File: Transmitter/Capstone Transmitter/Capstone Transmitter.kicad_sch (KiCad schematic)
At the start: 0 parts

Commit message: Started work on new schematics in KiCad
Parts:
- added BT1: Battery, Battery:BatteryHolder_Keystone_2479_3xAAA, symbol Device:Battery
- added C1, C2: C_Small, symbol Device:C_Small
- added U1: ESP32-C3-DevKitM-1, RF_Module:ESP32-C3-DevKitM-1, symbol RF_Module:ESP32-C3-DevKitM-1
- added U2: TPS63020DSJR, DSJ14_2P85X1P58, symbol TPS63020:TPS63020DSJR
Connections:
- new net: C1.1, C2.1, U2.10 (VIN), U2.11 (VIN)
- new net: U1.1 (GND), U1.12 (GND), U1.15 (GND), U1.16 (GND), U1.19 (GND), U1.24 (GND), U1.27 (GND), U1.30 (GND), U1.6 (GND), U1.8 (GND)
- new net: U1.13 (5V), U1.14 (5V)
- new net: U1.2 (3V3), U1.3 (3V3)
- new net +4.5V: BT1.1 (+)
- new net GND: BT1.2 (-)

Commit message: WIP remote
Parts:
- removed U1: ESP32-C3-DevKitM-1, RF_Module:ESP32-C3-DevKitM-1, symbol RF_Module:ESP32-C3-DevKitM-1
- added C10, C5, C6, C7, C8: 22u, symbol Device:C_Small
- added C11: 1U, symbol Device:C_Small
- added C3: 100n, symbol Device:C_Small
- added C4: 4p7, symbol Device:C_Small
- added C9: 0u1, symbol Device:C_Small
- added JP1: BootSel, symbol Jumper:Jumper_2_Small_Open
- added L1: 1u, symbol Device:L_Small
- added R1, R2: 1M, symbol Device:R_Small_US
- added R3: 68K, symbol Device:R_Small_US
- added R4: 180K, symbol Device:R_Small_US
- added R5: 10K, symbol Device:R_Small_US
- added U3: ESP32-WROOM-32UE, RF_Module:ESP32-WROOM-32UE, symbol RF_Module:ESP32-WROOM-32UE
- C1, C2: value C_Small -> 10u
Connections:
- net +4.5V: now also C1.1, C2.1, U2.10 (VIN), U2.11 (VIN)
- net GND: now also C1.2, C2.2, U2.15 (EPAD), U2.2 (GND), C10.2, C11.2, C3.2, C5.2, C6.2, C7.2, C8.2, C9.2, JP1.2 (B), R4.2, U3.[1,15,38,39] (GND)
- net EN: now reaches U2.1 (VINA)
- net EN: now also U2.12 (EN), C3.1
- net PS/SYNC: now reaches U2.13 (PS/SYNC)
- net at U2.14 (PG): now also R1.1
- net FB: now reaches U2.3 (FB)
- net FB: now also C4.2, R2.2, R4.1
- net +3.3V: now reaches U2.4 (VOUT)
- net +3.3V: now also U2.5 (VOUT), C10.1, C5.1, C6.1, C7.1, C8.1, C9.1, R1.2, R2.1, R3.1, R5.1, U3.2 (VDD)
- net L2: now reaches U2.6 (L2)
- net L2: now also U2.7 (L2), L1.2
- net L1: now reaches U2.8 (L1)
- net L1: now also U2.9 (L1), L1.1
- new net: JP1.1 (A), U3.25 (IO0)
- new net: C4.1, R3.2
- new net EN2: C11.1, R5.2, U3.3 (EN)
- new net UART_RX: U3.34 (RXD0/IO3)
- new net UART_TX: U3.35 (TXD0/IO1)
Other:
- moved on the sheet: BT1, C1, C2, U2

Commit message: Finished remote schematic, getting some sleep now
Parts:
- added J1, J2: Conn_01x04, symbol Connector_Generic:Conn_01x04
- added J3, J4, J5: Conn_01x02_Socket, symbol Connector:Conn_01x02_Socket
- added J6: AnalogStick Pot1 +/-, symbol Connector:Conn_01x02_Socket
- added J7: AnalogStick Pot2 +/-, symbol Connector:Conn_01x02_Socket
- added JP2: Pull up Jumper 1, symbol Jumper:Jumper_2_Small_Open
- added JP3: Pull up Jumper 2, symbol Jumper:Jumper_2_Small_Open
- added Q1: RevPolProt, symbol Transistor_FET:Q_PMOS_DGS
- added R6: 100K, symbol Device:R_Small_US
- added R7, R8: 10K, symbol Device:R_Small_US
- C11: value 1U -> 1u
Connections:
- net +3.3V: now also J1.1 (Pin_1), J6.1 (Pin_1), J7.1 (Pin_1), JP2.2 (B), JP3.2 (B)
- net +4.5V: now also Q1.3 (S); no longer BT1.1 (+)
- net GND: now also J1.4 (Pin_4), J6.2 (Pin_2), J7.2 (Pin_2), R6.2
- net UART_RX: now also J1.3 (Pin_3)
- net UART_TX: now also J1.2 (Pin_2)
- net JOY_BTN2: now reaches U3.11 (IO26)
- net JOY_BTN2: now also J5.1 (Pin_1)
- net JOY_BTN1: now reaches U3.12 (IO27)
- net JOY_BTN1: now also J5.2 (Pin_2)
- net JTAG_TMS: now reaches U3.13 (IO14)
- net JTAG_TMS: now also J2.1 (Pin_1)
- net JTAG_TDI: now reaches U3.14 (IO12)
- net JTAG_TDI: now also J2.2 (Pin_2)
- net JTAG_TCK: now reaches U3.16 (IO13)
- net JTAG_TCK: now also J2.3 (Pin_3)
- net JTAG_TDO: now reaches U3.23 (IO15)
- net JTAG_TDO: now also J2.4 (Pin_4)
- net JOY_X/LEFT: now reaches U3.6 (IO34)
- net JOY_X/LEFT: now also J3.1 (Pin_1), R8.1
- net JOY_Y/RIGHT: now reaches U3.7 (IO35)
- net JOY_Y/RIGHT: now also J3.2 (Pin_2), R7.1
- net JOY_UP: now reaches U3.8 (IO32)
- net JOY_UP: now also J4.1 (Pin_1)
- net JOY_DOWN: now reaches U3.9 (IO33)
- net JOY_DOWN: now also J4.2 (Pin_2)
- new net: JP2.1 (A), R8.2
- new net: BT1.1 (+), Q1.1 (D)
- new net: Q1.2 (G), R6.1
- new net: JP3.1 (A), R7.2
- no-connect marks 0 -> 13
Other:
- moved on the sheet: BT1, C10, C11, C9, JP1, R5, U3

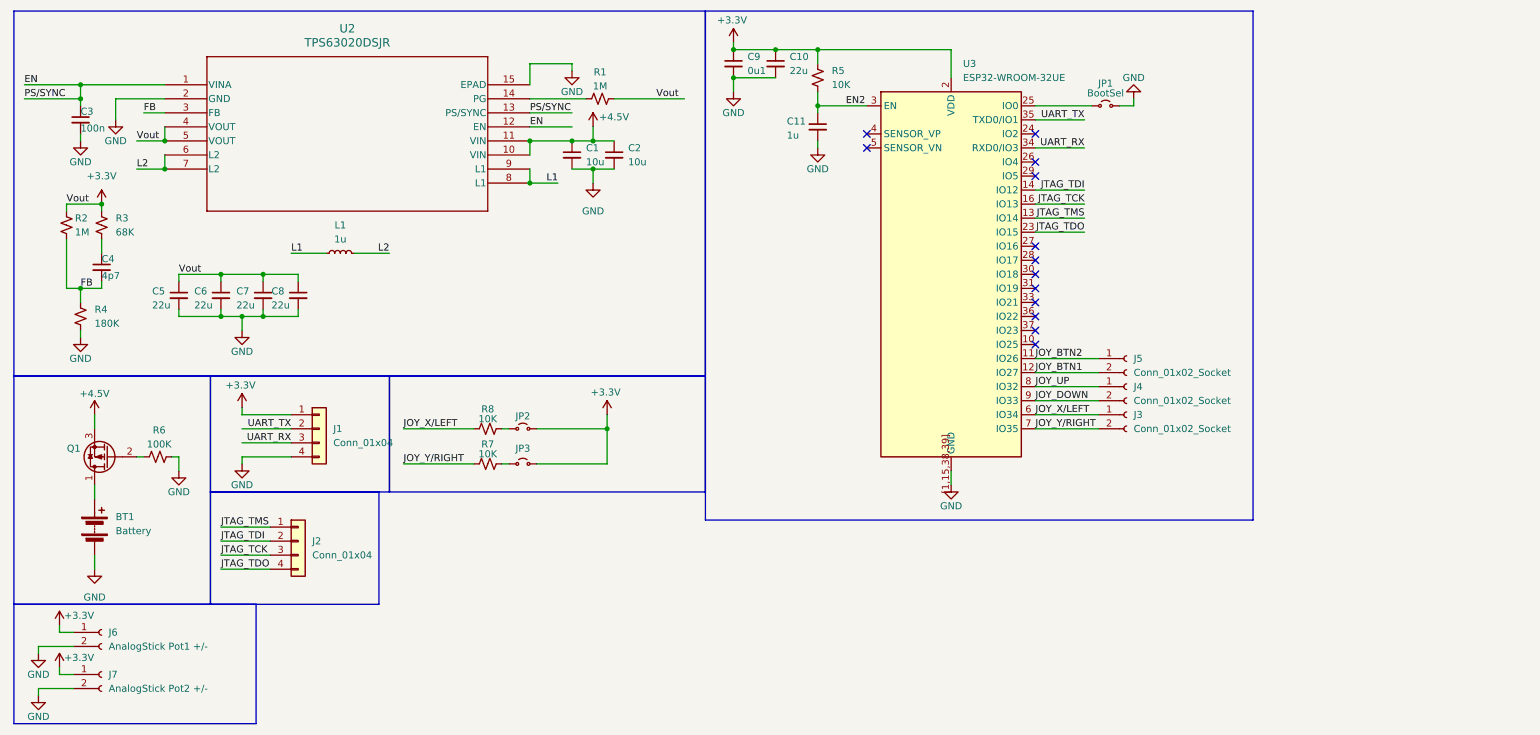
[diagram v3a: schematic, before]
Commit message: Added schematic markings
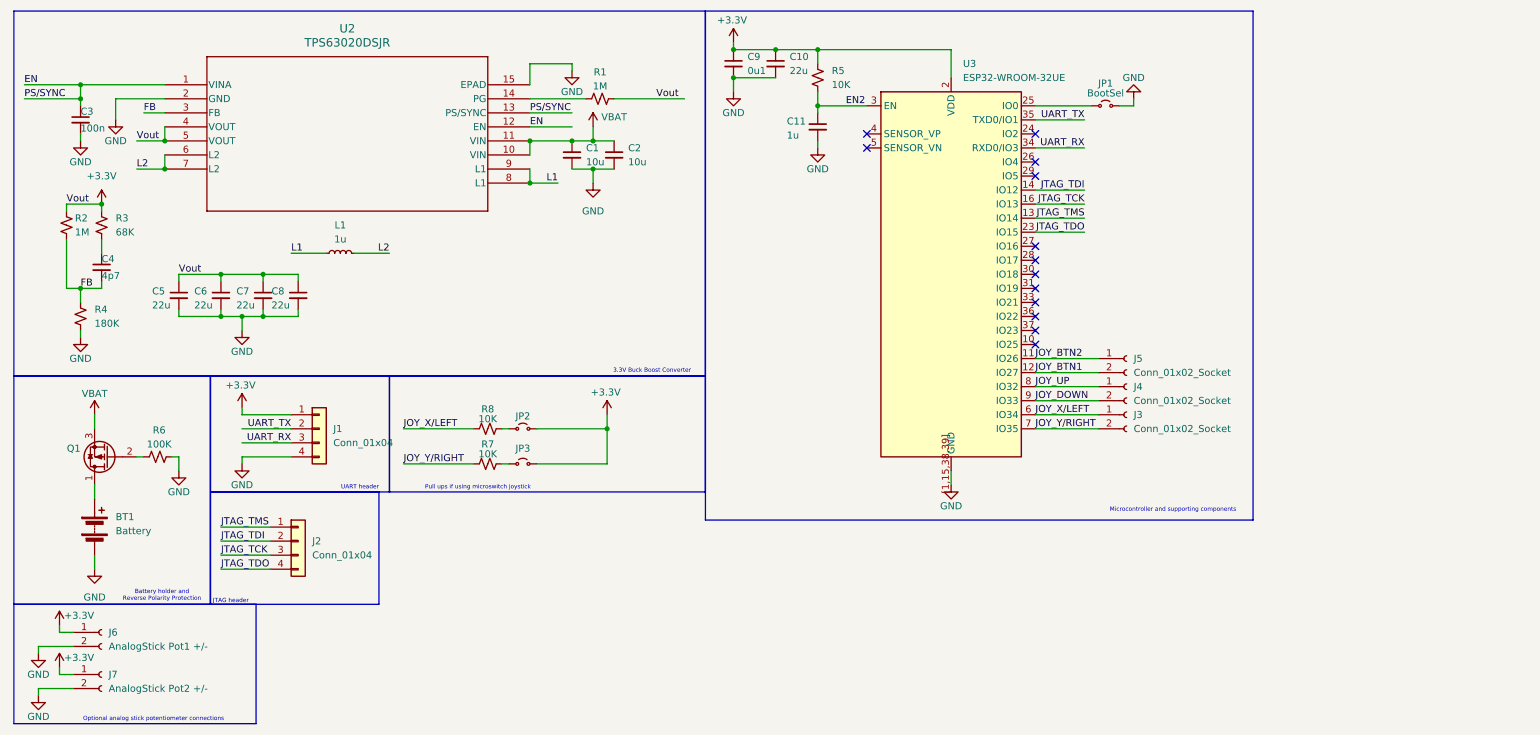
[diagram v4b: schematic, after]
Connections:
- net +4.5V renamed VBAT
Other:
- note added: "3.3V Buck Boost Converter"
- note added: "Battery holder and Reverse Polarity Protection"
- note added: "JTAG header"
- note added: "Microcontroller and supporting components"
- note added: "Optional analog stick potentiometer connections"
- note added: "Pull ups if using microswitch joystick"
- note added: "UART header"
- company: (none) -> UMass Lowell
- title: (none) -> Capstone Remote
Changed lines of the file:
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@@
 	(generator_version "10.0")
 	(paper "A4")
+	(title_block
+		(title "Capstone Remote")
+		(date "2026-09-13")
+		(rev "1")
+		(company "UMass Lowell")
+	)
 	(rectangle
 		(start 137.16 12.065)
@@
 		)
 	)
+	(text "UART header"
+		(exclude_from_sim no)
+		(at 74.676 98.298 0)
+		(effects
+			(font
+				(size 0.762 0.762)
+			)
+		)
+	)
+	(text "Battery holder and\nReverse Polarity Protection"
+		(exclude_from_sim no)
+		(at 38.862 117.856 0)
+		(effects
+			(font
+				(size 0.762 0.762)
+			)
+		)
+	)
+	(text "3.3V Buck Boost Converter"
+		(exclude_from_sim no)
+		(at 127.508 77.216 0)
+		(effects
+			(font
+				(size 0.762 0.762)
+			)
+		)
+	)
+	(text "Pull ups if using microswitch joystick"
+		(exclude_from_sim no)
+		(at 96.012 98.298 0)
+		(effects
+			(font
+				(size 0.762 0.762)
+			)
+		)
+	)
+	(text "Microcontroller and supporting components"
+		(exclude_from_sim no)
+		(at 221.742 102.362 0)
+		(effects
+			(font
+				(size 0.762 0.762)
+			)
+		)
+	)
+	(text "JTAG header"
+		(exclude_from_sim no)
+		(at 51.308 118.872 0)
+		(effects
+			(font
+				(size 0.762 0.762)
+			)
+		)
+	)
+	(text "Optional analog stick potentiometer connections"
+		(exclude_from_sim no)
+		(at 37.338 140.208 0)
+		(effects
+			(font
+				(size 0.762 0.762)
+			)
+		)
+	)
 	(junction
 		(at 49.53 59.69)
@@
 			)
 		)
-		(property "Value" "+4.5V"
+		(property "Value" "VBAT"
 			(at 120.65 31.242 0)
 			(show_name no)
@@
 			)
 		)
-		(property "Value" "+4.5V"
+		(property "Value" "VBAT"
 			(at 26.67 81.28 0)
 			(show_name no)

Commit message: Fixed pull up resistors
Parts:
- added R10, R11, R12, R9: 10K, symbol Device:R_Small_US
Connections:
- net +3.3V: now also R10.2, R11.2, R12.2, R9.2
- net JOY_BTN1: now also R11.1
- net JOY_BTN2: now also R12.1
- net JOY_DOWN: now also R9.1
- net JOY_UP: now also R10.1
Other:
- note added: "Pull ups"
- note removed: "Pull ups if using microswitch joystick"
